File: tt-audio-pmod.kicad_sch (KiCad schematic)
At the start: 18 parts, among them J1 10129382-912001BLF, J2 Conn_02x06_Top_Bottom, J4 Conn_01x03, J5 PJ-320B, U1 74LVCE1G126SE-7

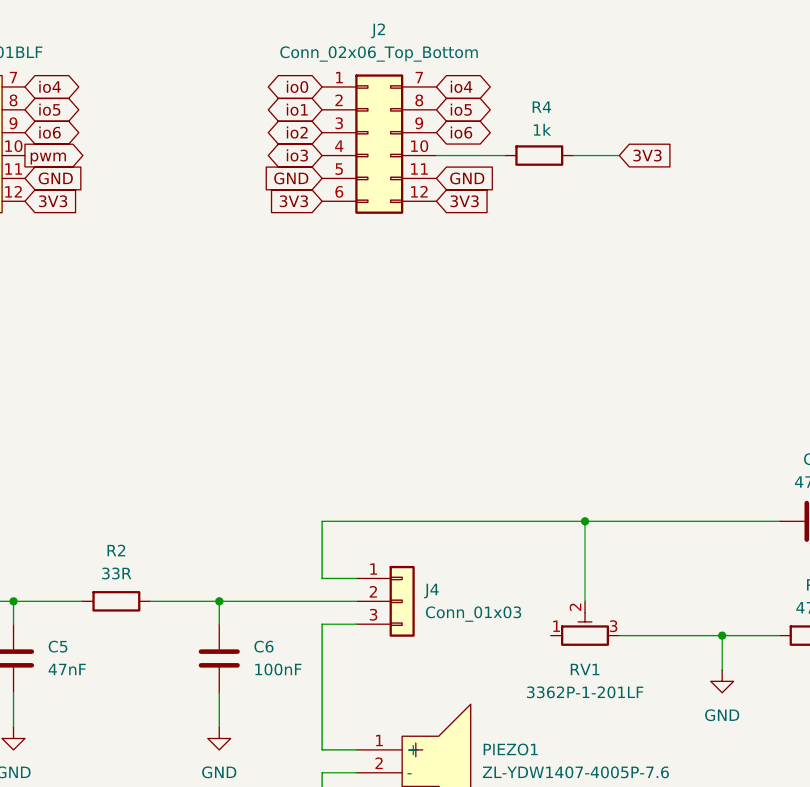
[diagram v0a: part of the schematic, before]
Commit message: Silkscreen and BOM updates
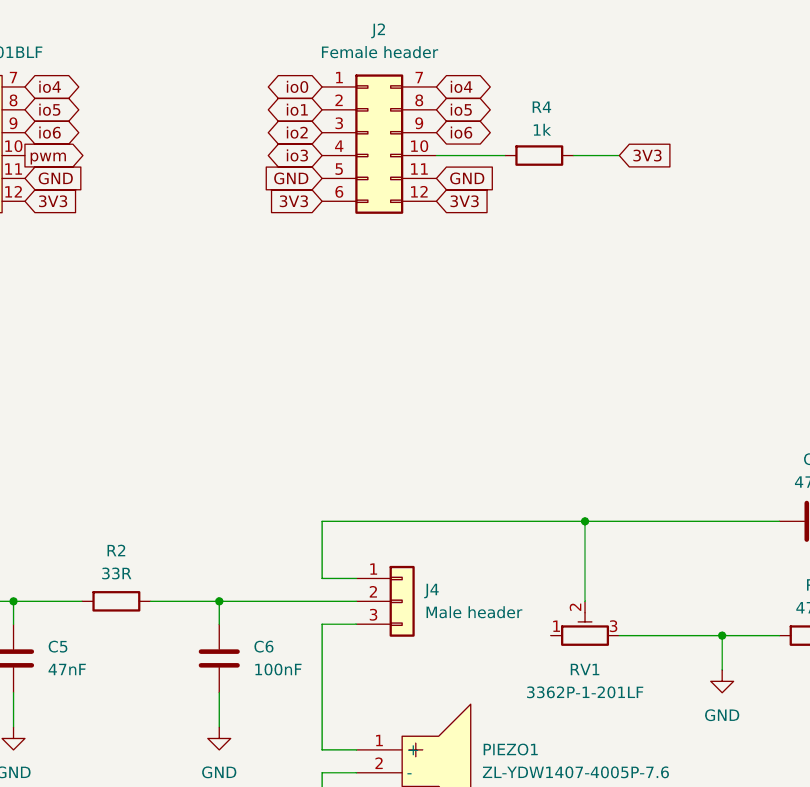
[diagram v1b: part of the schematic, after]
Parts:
- C1, C4, C6: LCSC Part (none) -> C14663
- C2: LCSC Part (none) -> C16780
- C3: LCSC Part (none) -> C15850
- C5: LCSC Part (none) -> C1622
- J1: LCSC Part C492434 -> C60565
- J2: value Conn_02x06_Top_Bottom -> Female header; LCSC Part (none) -> C92269
- J4: value Conn_01x03 -> Male header; LCSC Part (none) -> C49257
- J5: LCSC Part (none) -> C2884998
- L1: LCSC Part (none) -> C2941578
- R1: LCSC Part (none) -> C22787
- R2: LCSC Part (none) -> C23140
- R3: LCSC Part (none) -> C23179
- R4: LCSC Part (none) -> C21190
- RV1: LCSC Part (none) -> C124581
- U1: LCSC Part (none) -> C842506
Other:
- title: Tiny Tapeout Audio PMOD -> ${TITLE}
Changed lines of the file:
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@@
 	(paper "A4")
 	(title_block
-		(title "Tiny Tapeout Audio PMOD")
-		(rev "1.0")
+		(title "${TITLE}")
+		(rev "${REVISION}")
 	)
 	(junction
@@
 		(property "Description" "Inductor"
 			(at 76.2 82.55 0)
+			(effects
+				(font
+					(size 1.27 1.27)
+				)
+				(hide yes)
+			)
+		)
+		(property "LCSC Part" "C2941578"
+			(at 76.2 82.55 90)
 			(effects
 				(font
@@
 			)
 		)
+		(property "LCSC Part" "C1622"
+			(at 116.84 110.49 0)
+			(effects
+				(font
+					(size 1.27 1.27)
+				)
+				(hide yes)
+			)
+		)
 		(pin "1"
 		)
@@
 			)
 		)
+		(property "LCSC Part" "C22787"
+			(at 95.25 104.14 90)
+			(effects
+				(font
+					(size 1.27 1.27)
+				)
+				(hide yes)
+			)
+		)
 		(pin "2"
 		)
@@
 			)
 		)
+		(property "LCSC Part" "C21190"
+			(at 175.26 54.61 90)
+			(effects
+				(font
+					(size 1.27 1.27)
+				)
+				(hide yes)
+			)
+		)
 		(pin "2"
 		)
@@
 			)
 		)
-		(property "Value" "Conn_02x06_Top_Bottom"
+		(property "Value" "Female header"
 			(at 157.48 43.18 0)
 			(effects
@@
 		)
 		(property "Description" "Generic connector, double row, 02x06, top/bottom pin numbering scheme (row 1: 1...pins_per_row, row2: pins_per_row+1 ... num_pins), script generated (kicad-library-utils/schlib/autogen/connector/)"
+			(at 156.21 52.07 0)
+			(effects
+				(font
+					(size 1.27 1.27)
+				)
+				(hide yes)
+			)
+		)
+		(property "LCSC Part" "C92269"
 			(at 156.21 52.07 0)
 			(effects
@@
 			)
 		)
+		(property "LCSC Part" "C14663"
+			(at 45.72 86.36 0)
+			(effects
+				(font
+					(size 1.27 1.27)
+				)
+				(hide yes)
+			)
+		)
 		(pin "2"
 		)
@@
 			)
 		)
+		(property "LCSC Part" "C23179"
+			(at 205.74 107.95 90)
+			(effects
+				(font
+					(size 1.27 1.27)
+				)
+				(hide yes)
+			)
+		)
 		(pin "2"
 		)
@@
 			)
 		)
-		(property "LCSC Part" "C492434"
+		(property "LCSC Part" "C60565"
 			(at 110.4438 68.0299 0)
 			(effects
@@
 			)
 		)
+		(property "LCSC Part" "C16780"
+			(at 205.74 95.25 90)
+			(effects
+				(font
+					(size 1.27 1.27)
+				)
+				(hide yes)
+			)
+		)
 		(pin "2"
 		)
@@
 			)
 		)
+		(property "LCSC Part" "C15850"
+			(at 31.75 86.36 0)
+			(effects
+				(font
+					(size 1.27 1.27)
+				)
+				(hide yes)
+			)
+		)
 		(pin "2"
 		)
@@
 			)
 		)
+		(property "LCSC Part" "C124581"
+			(at 180.34 107.95 90)
+			(effects
+				(font
+					(size 1.27 1.27)
+				)
+				(hide yes)
+			)
+		)
 		(pin "2"
 		)
@@
 		)
 		(property "Description" "Single Buffer Gate Tri-State, Low-Voltage CMOS"
+			(at 66.04 104.14 0)
+			(effects
+				(font
+					(size 1.27 1.27)
+				)
+				(hide yes)
+			)
+		)
+		(property "LCSC Part" "C842506"
 			(at 66.04 104.14 0)
 			(effects
@@
 			)
 		)
+		(property "LCSC Part" "C23140"
+			(at 128.27 104.14 90)
+			(effects
+				(font
+					(size 1.27 1.27)
+				)
+				(hide yes)
+			)
+		)
 		(pin "2"
 		)
@@
 				)
 				(justify bottom)
+				(hide yes)
+			)
+		)
+		(property "LCSC Part" "C2884998"
+			(at 240.03 101.6 0)
+			(effects
+				(font
+					(size 1.27 1.27)
+				)
 				(hide yes)
 			)
@@
 			)
 		)
+		(property "LCSC Part" "C14663"
+			(at 104.14 110.49 0)
+			(effects
+				(font
+					(size 1.27 1.27)
+				)
+				(hide yes)
+			)
+		)
 		(pin "1"
 		)
@@
 			)
 		)
+		(property "LCSC Part" "C14663"
+			(at 139.7 110.49 0)
+			(effects
+				(font
+					(size 1.27 1.27)
+				)
+				(hide yes)
+			)
+		)
 		(pin "1"
 		)
@@
 			)
 		)
-		(property "Value" "Conn_01x03"
+		(property "Value" "Male header"
 			(at 162.56 105.4099 0)
 			(effects
@@
 			(at 160.02 104.14 0)
 			(effects
+				(font
+					(size 1.27 1.27)
+				)
+				(hide yes)
+			)
+		)
+		(property "LCSC Part" "C49257"
+			(at 160.02 104.14 0)
+			(effects
